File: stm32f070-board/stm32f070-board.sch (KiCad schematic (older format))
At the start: 39 parts

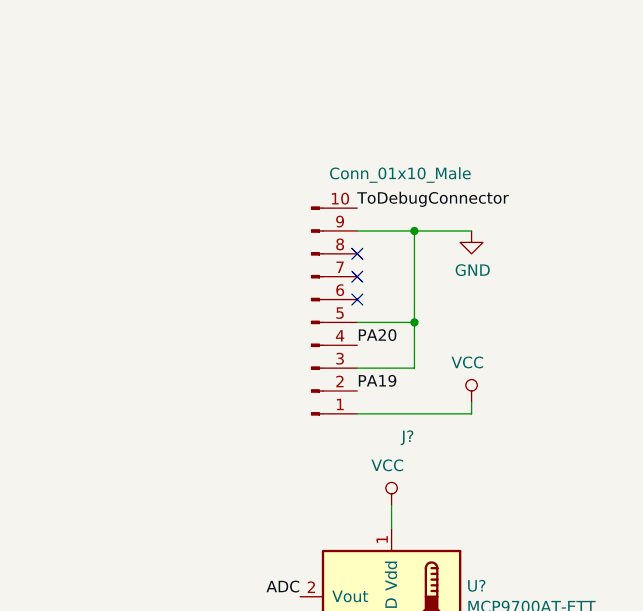
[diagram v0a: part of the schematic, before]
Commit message: replaced 10pin debug connector by 5 pin debug connector - removed redundant pins.
Signed-off-by: suyash <in.suyash@gmail.com>
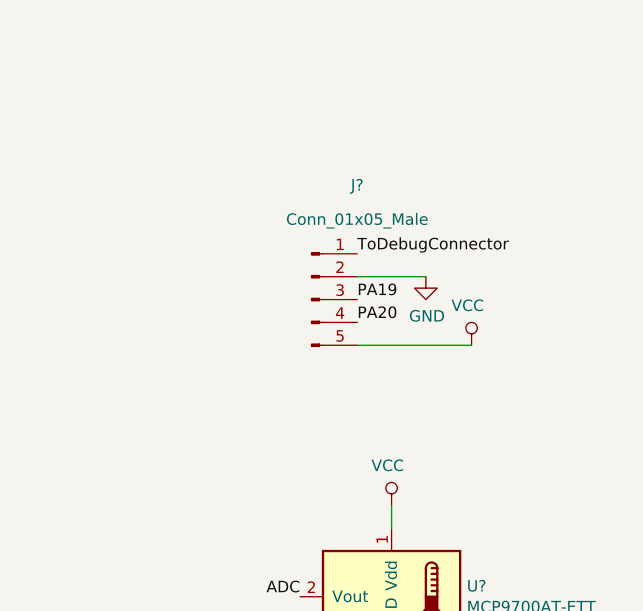
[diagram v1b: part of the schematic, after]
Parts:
- removed J?: Conn_01x10_Male, symbol Connector:Conn_01x10_Male
- added J?: Conn_01x05_Male, symbol Connector:Conn_01x05_Male
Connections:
- net GND: now also J?.2 (Pin_2)
- net PA19: now also J?.3 (Pin_3)
- net PA20: now also J?.4 (Pin_4)
- net ToDebugConnector: now also J?.1 (Pin_1)
- net VCC: now also J?.5 (Pin_5)
- no-connect marks 14 -> 11
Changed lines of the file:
@@
 Text Label 5750 1150 1    50   ~ 0
 VDDA
-$Comp
-L Connector:Conn_01x10_Male J?
-U 1 1 5D7BCD4D
-P 9600 2150
-F 0 "J?" H 10050 2650 50  0000 R CNN
-F 1 "Conn_01x10_Male" H 10300 1500 50  0000 R CNN
-F 2 "" H 9600 2150 50  0001 C CNN
-F 3 "~" H 9600 2150 50  0001 C CNN
-	1    9600 2150
-	1    0    0    1
-$EndComp
 Text Label 6500 3550 0    50   ~ 0
 PA20
 Text Label 6500 3350 0    50   ~ 0
 PA19
-Text Label 9800 2450 0    50   ~ 0
-PA19
-Text Label 9800 2250 0    50   ~ 0
-PA20
-NoConn ~ 9800 1850
-NoConn ~ 9800 1950
-NoConn ~ 9800 2050
-Wire Wire Line
-	9800 1750 10050 1750
-Wire Wire Line
-	10050 1750 10050 2150
-Wire Wire Line
-	10050 2150 9800 2150
-Wire Wire Line
-	10050 2150 10050 2350
-Wire Wire Line
-	10050 2350 9800 2350
-Connection ~ 10050 2150
-$Comp
-L power:GND #PWR?
-U 1 1 5D7C4203
-P 10300 1750
-F 0 "#PWR?" H 10300 1500 50  0001 C CNN
-F 1 "GND" H 10305 1577 50  0000 C CNN
-F 2 "" H 10300 1750 50  0001 C CNN
-F 3 "" H 10300 1750 50  0001 C CNN
-	1    10300 1750
-	1    0    0    -1
-$EndComp
-Wire Wire Line
-	10050 1750 10300 1750
-Connection ~ 10050 1750
-$Comp
-L power:VCC #PWR?
-U 1 1 5D7C5A36
-P 10300 2500
-F 0 "#PWR?" H 10300 2350 50  0001 C CNN
-F 1 "VCC" H 10317 2673 50  0000 C CNN
-F 2 "" H 10300 2500 50  0001 C CNN
-F 3 "" H 10300 2500 50  0001 C CNN
-	1    10300 2500
-	-1   0    0    -1
-$EndComp
-Wire Wire Line
-	9800 2550 10300 2550
-Wire Wire Line
-	10300 2550 10300 2500
-Text Label 9800 1650 0    50   ~ 0
-ToDebugConnector
 NoConn ~ 1600 3650
 Text Label 1600 3450 0    50   ~ 0
@@
 Wire Wire Line
 	5150 3550 5200 3550
+$Comp
+L Connector:Conn_01x05_Male J?
+U 1 1 5D7FD58A
+P 9600 2050
+F 0 "J?" H 9800 2550 50  0000 C CNN
+F 1 "Conn_01x05_Male" H 9800 2400 50  0000 C CNN
+F 2 "" H 9600 2050 50  0001 C CNN
+F 3 "~" H 9600 2050 50  0001 C CNN
+	1    9600 2050
+	1    0    0    -1
+$EndComp
+Text Label 9800 1850 0    50   ~ 0
+ToDebugConnector
+$Comp
+L power:GND #PWR?
+U 1 1 5D7FDC89
+P 10100 1950
+F 0 "#PWR?" H 10100 1700 50  0001 C CNN
+F 1 "GND" H 10105 1777 50  0000 C CNN
+F 2 "" H 10100 1950 50  0001 C CNN
+F 3 "" H 10100 1950 50  0001 C CNN
+	1    10100 1950
+	1    0    0    -1
+$EndComp
+Wire Wire Line
+	9800 1950 10100 1950
+$Comp
+L power:VCC #PWR?
+U 1 1 5D8010D4
+P 10300 2250
+F 0 "#PWR?" H 10300 2100 50  0001 C CNN
+F 1 "VCC" H 10317 2423 50  0000 C CNN
+F 2 "" H 10300 2250 50  0001 C CNN
+F 3 "" H 10300 2250 50  0001 C CNN
+	1    10300 2250
+	-1   0    0    -1
+$EndComp
+Wire Wire Line
+	9800 2250 10300 2250
+Text Label 9800 2050 0    50   ~ 0
+PA19
+Text Label 9800 2150 0    50   ~ 0
+PA20
 $EndSCHEMATC

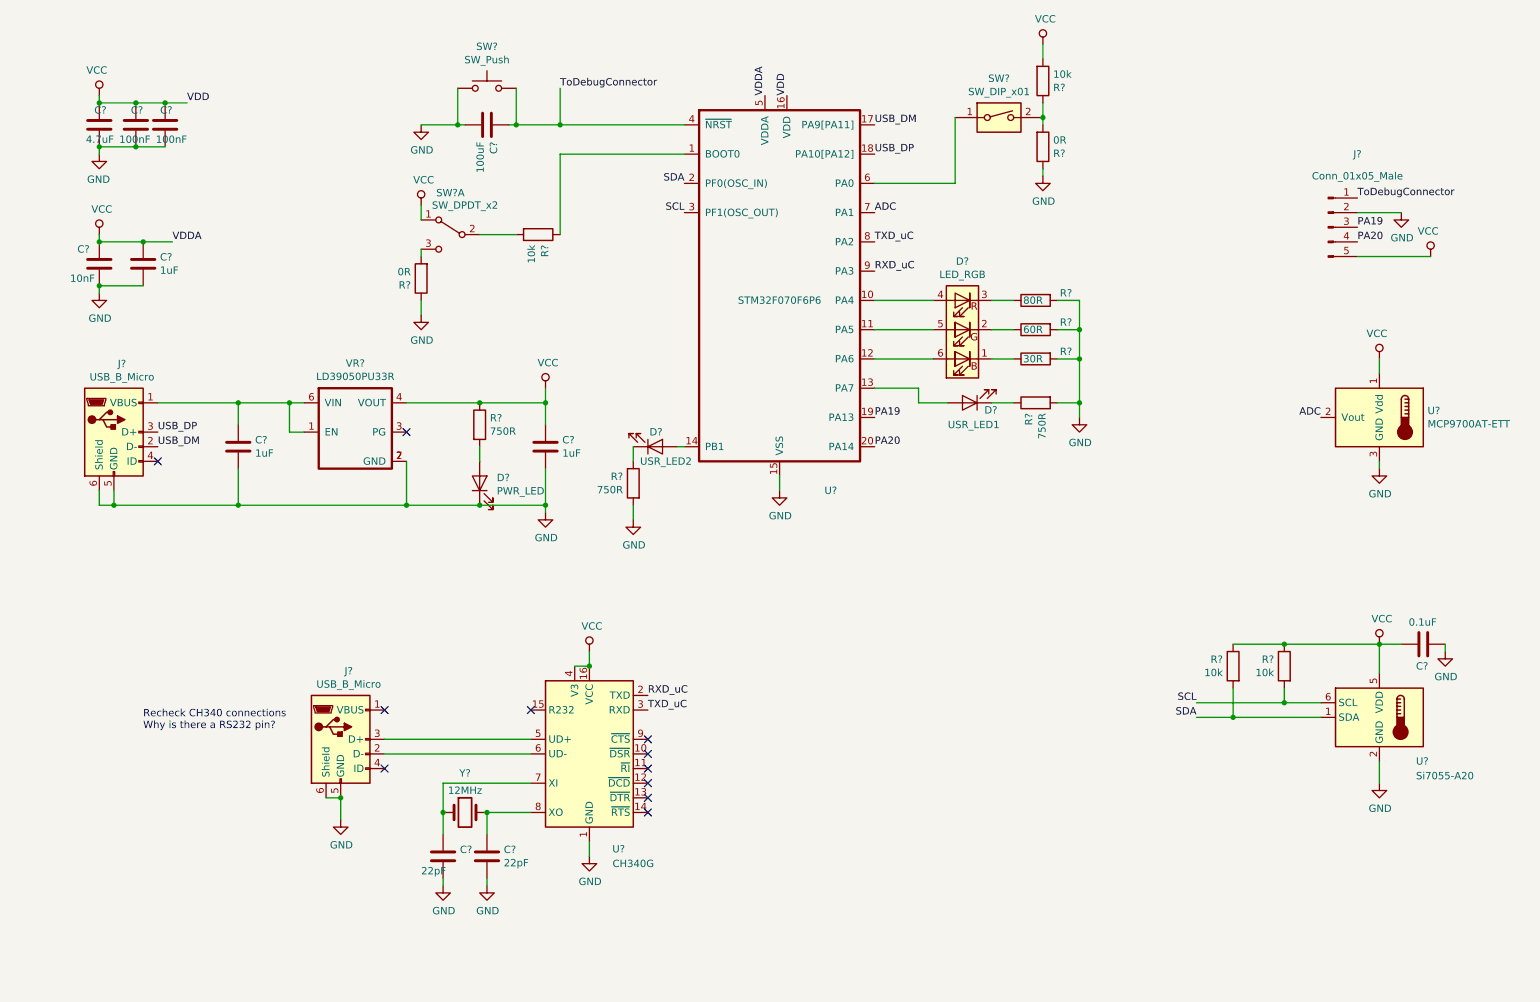
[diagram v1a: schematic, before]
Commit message: annoted the schematic
Signed-off-by: suyash <in.suyash@gmail.com>
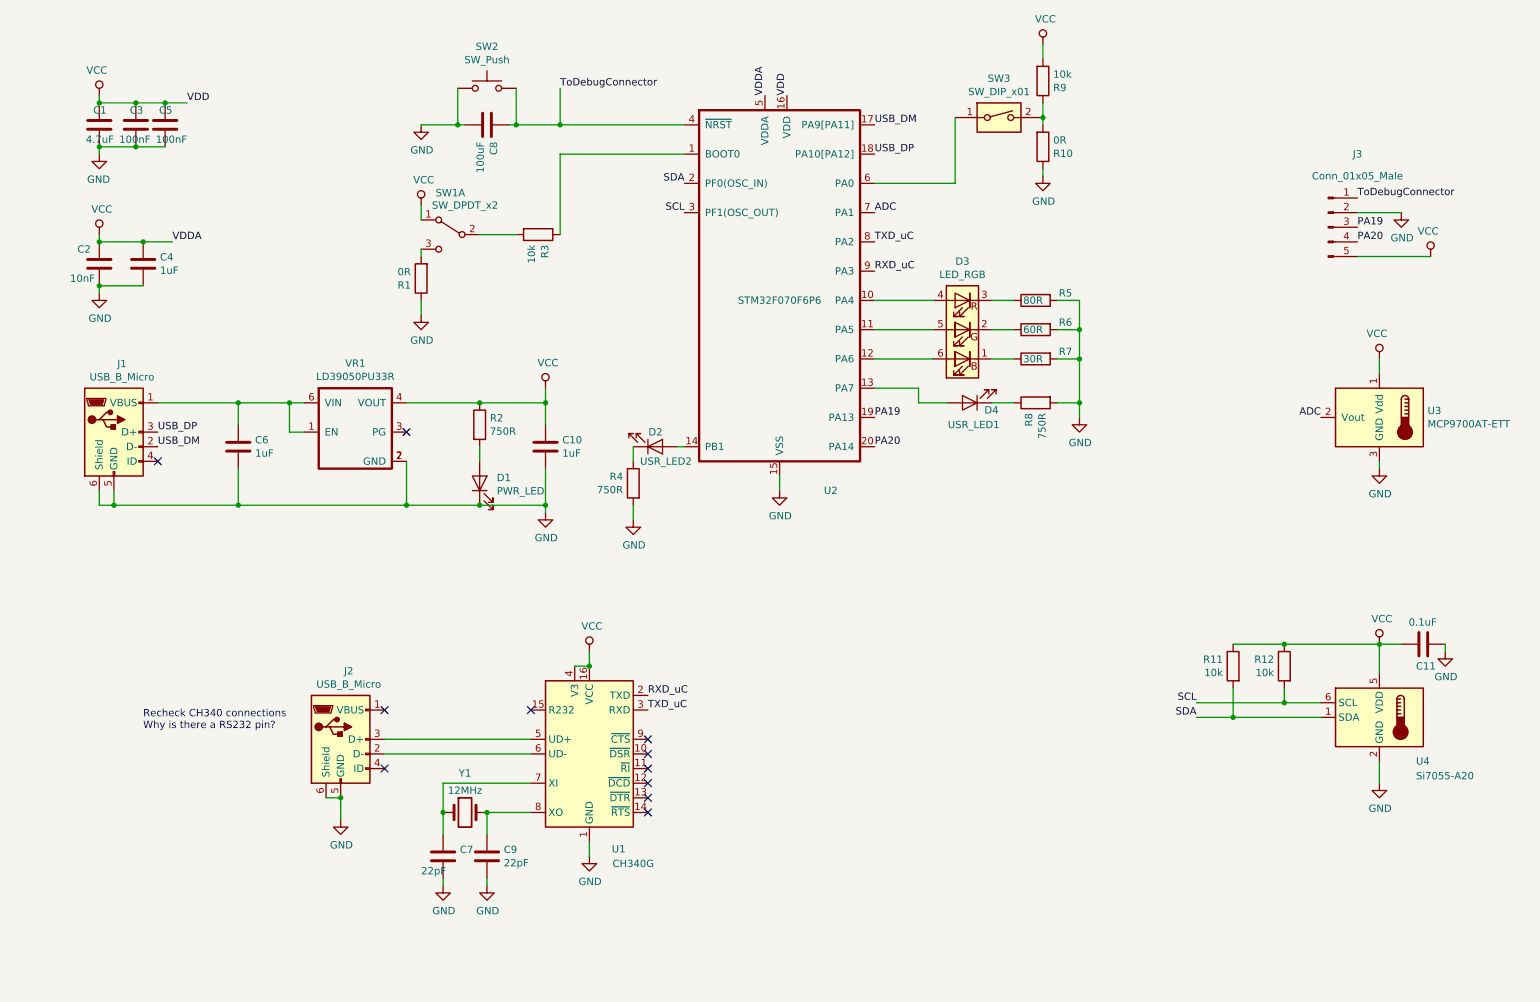
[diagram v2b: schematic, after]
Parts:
- gave numbers to parts that had none: 39

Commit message: Added datasheet and product pages to the components
Signed-off-by: suyash <in.suyash@gmail.com>
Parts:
- C1: Vendor (none) -> https://in.element14.com/walsin/0603f475z100ct/cap-4-7-f-10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
- C10, C4, C6: Vendor (none) -> https://in.element14.com/multicomp/mc0603x105k100ct/cap-1-f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
- C11, C3, C5: Vendor (none) -> https://in.element14.com/multicomp/mc0603b104m500ct/ceramic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
- C2: Vendor (none) -> https://in.element14.com/multicomp/mc0603b103m500ct/ceramic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
- C7, C9: Vendor (none) -> https://in.element14.com/walsin/0603n220j500ct/cap-22pf-50v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
- C8: Vendor (none) -> Use 4.7uF if you don't find 100uF in local market
- D1, D2, D4: Vendor (none) -> https://in.element14.com/vishay/tlms1000-gs08/led-0603-red-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
- D3: Vendor (none) -> https://in.element14.com/cree/clx6f-fkc-cnp1st1e1bb7d3d3/le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
- J1, J2: Vendor (none) -> https://robu.in/product/micro-usb-2-0-b-type-5-pin-connecto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
- J3: Vendor (none) -> https://in.element14.com/harwin/m52-040023v0545/header-tht-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
- R1, R10: Vendor (none) -> https://in.element14.com/walsin/wr06x000-ptl/res-0r0-0603-t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
- R11, R12, R3, R9: Vendor (none) -> https://in.element14.com/walsin/wr06x1002ftl/res-10k-1-75v-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
- R2, R4, R8: Vendor (none) -> https://in.element14.com/multicomp/mcwr06x7500ftl/res-750r-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
- R5: Vendor (none) -> https://in.element14.com/multicomp/mcwr06x82r0ftl/res-82r-1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
- R6: Vendor (none) -> https://in.element14.com/multicomp/mcwr06x62r0ftl/res-62r-1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
- R7: Vendor (none) -> https://in.element14.com/walsin/wr06x30r0ftl/res-30r-1-0-1w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
- SW1: Vendor (none) -> https://in.element14.com/c-k-components/js202011jcqn/slide-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
- SW2, SW3: Vendor (none) -> https://robu.in/product/362-5mm-tactile-push-button-switch-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
- U1: Vendor (none) -> https://robu.in/product/ch340g-soic16-usb-to-serial-ttl-rs2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
- U2: Vendor (none) -> https://in.element14.com/stmicroelectronics/stm32f070f6p6tr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
- U3: Vendor (none) -> https://in.element14.com/microchip/mcp9700at-e-tt/sensor-te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
- U4: Vendor (none) -> https://in.element14.com/silicon-labs/si7055-a20-imr/temp-s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
- VR1: Vendor (none) -> https://in.element14.com/stmicroelectronics/ld39050pu33r/ld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
- Y1: Vendor (none) -> https://in.element14.com/abracon/abls-12-000mhz-b4-t/crysta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
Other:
- note added: "Check for correct dimentions of SW2, SW3\nCorrect schematic symbol of SW3\n\n"
- note added: "Replace C8 with 4.7uF if you dont get 100uF."

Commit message: Changed the user switch SW3 to toggle switch
Signed-off-by: suyash <in.suyash@gmail.com>
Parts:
- removed SW3: SW_DIP_x01, symbol Switch:SW_DIP_x01
- added SW3: SW_Push, symbol Switch:SW_Push
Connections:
- net at U2.6 (PA0): now also SW3.1
- net at R10.2, R9.1: now also SW3.2
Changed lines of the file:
@@
 	2750 5950 2850 5950
 Connection ~ 2850 5950
-Wire Wire Line
-	7650 1300 7650 1200
-$Comp
-L Switch:SW_DIP_x01 SW3
-U 1 1 5D7CAFC7
-P 7350 1300
-F 0 "SW3" H 7350 1567 50  0000 C CNN
-F 1 "SW_DIP_x01" H 7350 1476 50  0000 C CNN
-F 2 "" H 7350 1300 50  0001 C CNN
-F 3 "" H 7350 1300 50  0001 C CNN
-F 4 "https://robu.in/product/362-5mm-tactile-push-button-switch-20pcs/" H 7350 1300 50  0001 C CNN "Vendor"
-	1    7350 1300
-	1    0    0    -1
-$EndComp
 $Comp
 L Device:R R10
@@
 Wire Wire Line
 	7650 1700 7650 1650
-Wire Wire Line
-	7650 1350 7650 1300
-Connection ~ 7650 1300
 $Comp
 L Switch:SW_DPDT_x2 SW1
@@
 Text Notes 1950 1650 0    50   ~ 0
 Replace C8 with 4.7uF if you dont get 100uF.
+Wire Wire Line
+	7650 1200 7650 1300
+$Comp
+L Switch:SW_Push SW3
+U 1 1 5D8E3013
+P 7350 1300
+F 0 "SW3" H 7350 1585 50  0000 C CNN
+F 1 "SW_Push" H 7350 1494 50  0000 C CNN
+F 2 "" H 7350 1500 50  0001 C CNN
+F 3 "" H 7350 1500 50  0001 C CNN
+F 4 "https://robu.in/product/362-5mm-tactile-push-button-switch-20pcs/" H 7350 1300 50  0001 C CNN "Vendor"
+	1    7350 1300
+	1    0    0    -1
+$EndComp
+Wire Wire Line
+	7550 1300 7650 1300
+Connection ~ 7650 1300
+Wire Wire Line
+	7650 1300 7650 1350
+Wire Wire Line
+	7150 1300 7050 1300
 $EndSCHEMATC

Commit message: Moved all the notes to bottom left of the sheet.
Signed-off-by: suyash <in.suyash@gmail.com>
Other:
- note added: "Note: \n- Recheck RS232 pin connection on CH340\n- Replace C8 with 4.7uF if you don't get 100uF\n- Check for correct dimentions of SW2, SW3\n"
- note removed: "Check for correct dimentions of SW2, SW3\nCorrect schematic symbol of SW3\n\n"
- note removed: "Recheck CH340 connections\nWhy is there a RS232 pin?\n\n\n"
- note removed: "Replace C8 with 4.7uF if you dont get 100uF."
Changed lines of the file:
@@
 Wire Wire Line
 	2850 6100 2850 5950
-Text Notes 1500 5650 0    50   ~ 0
-Recheck CH340 connections\nWhy is there a RS232 pin?\n\n\n
 $Comp
 L Device:Crystal Y1
@@
 Wire Wire Line
 	1300 3950 1300 3850
-Text Notes 3450 850  0    50   ~ 0
-Check for correct dimentions of SW2, SW3\nCorrect schematic symbol of SW3\n\n
-Text Notes 1950 1650 0    50   ~ 0
-Replace C8 with 4.7uF if you dont get 100uF.
 Wire Wire Line
 	7650 1200 7650 1300
@@
 Wire Wire Line
 	7150 1300 7050 1300
+Text Notes 600  7250 0    50   ~ 0
+Note: \n- Recheck RS232 pin connection on CH340\n- Replace C8 with 4.7uF if you don't get 100uF\n- Check for correct dimentions of SW2, SW3\n
 $EndSCHEMATC

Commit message: fixed broken link to product page for 0.1uF capacitor
Signed-off-by: suyash <in.suyash@gmail.com>
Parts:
- C11: Vendor https://in.element14.com/multicomp/mc0603b104m500ct/ceramic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 -> https://in.element14.com/multicomp/mc0603b104m160ct/ceramic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
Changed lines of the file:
@@
 F 2 "" H 10288 4750 50  0001 C CNN
 F 3 "http://www.farnell.com/datasheets/1522998.pdf" H 10250 4900 50  0001 C CNN
-F 4 "https://in.element14.com/multicomp/mc0603b104m500ct/ceramic-capacitor-0-1uf-50v-x7r/dp/170995" H 0   0   50  0001 C CNN "Vendor"
+F 4 "https://in.element14.com/multicomp/mc0603b104m160ct/ceramic-capacitor-0-1uf-16v-x7r/dp/1709956?ost=MC0603B104M160CT&ddkey=https%3Aen-IN%2FElement14_India%2Fsearch" H 0   0   50  0001 C CNN "Vendor"
 	1    10250 4900
 	0    1    1    0

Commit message: Added footprints to passive components
Signed-off-by: suyash <in.suyash@gmail.com>
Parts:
- C1, C10, C11, C2, C3, C4, C5, C6, C7, C8, C9: footprint (none) -> Capacitor_SMD:C_0603_1608Metric_Pad1.05x0.95mm_HandSolder
- R1, R10, R11, R12, R2, R3, R4, R5, R6, R7, R8, R9: footprint (none) -> Resistor_SMD:R_0603_1608Metric_Pad1.05x0.95mm_HandSolder

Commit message: added led footprints
Signed-off-by: suyash <in.suyash@gmail.com>
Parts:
- D1, D2, D4: footprint (none) -> stm32f070-board:LED_VISHAY
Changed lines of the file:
@@
 F 0 "D1" V 3838 3683 50  0000 R CNN
 F 1 "PWR_LED" V 3747 3683 50  0000 R CNN
-F 2 "" H 3800 3800 50  0001 C CNN
+F 2 "stm32f070-board:LED_VISHAY" H 3800 3800 50  0001 C CNN
 F 3 "http://www.farnell.com/datasheets/2049859.pdf" H 3800 3800 50  0001 C CNN
 F 4 "https://in.element14.com/vishay/tlms1000-gs08/led-0603-red-4mcd-628nm/dp/1328308?ost=1328308&ddkey=https%3Aen-IN%2FElement14_India%2Fsearch" V 3800 3800 50  0001 C CNN "Vendor"
@@
 F 0 "D4" H 7050 3300 50  0000 R CNN
 F 1 "USR_LED1" H 7300 3400 50  0000 R CNN
-F 2 "" H 7150 3250 50  0001 C CNN
+F 2 "stm32f070-board:LED_VISHAY" H 7150 3250 50  0001 C CNN
 F 3 "http://www.farnell.com/datasheets/2049859.pdf" H 7150 3250 50  0001 C CNN
 F 4 "https://in.element14.com/vishay/tlms1000-gs08/led-0603-red-4mcd-628nm/dp/1328308?ost=1328308&ddkey=https%3Aen-IN%2FElement14_India%2Fsearch" H 7150 3250 50  0001 C CNN "Vendor"
@@
 F 0 "D2" H 5050 3450 50  0000 R CNN
 F 1 "USR_LED2" H 5250 3650 50  0000 R CNN
-F 2 "" H 5000 3550 50  0001 C CNN
+F 2 "stm32f070-board:LED_VISHAY" H 5000 3550 50  0001 C CNN
 F 3 "http://www.farnell.com/datasheets/2049859.pdf" H 5000 3550 50  0001 C CNN
 F 4 "https://in.element14.com/vishay/tlms1000-gs08/led-0603-red-4mcd-628nm/dp/1328308?ost=1328308&ddkey=https%3Aen-IN%2FElement14_India%2Fsearch" H 5000 3550 50  0001 C CNN "Vendor"
